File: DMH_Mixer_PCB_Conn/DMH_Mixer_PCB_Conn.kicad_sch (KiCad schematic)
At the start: 0 parts

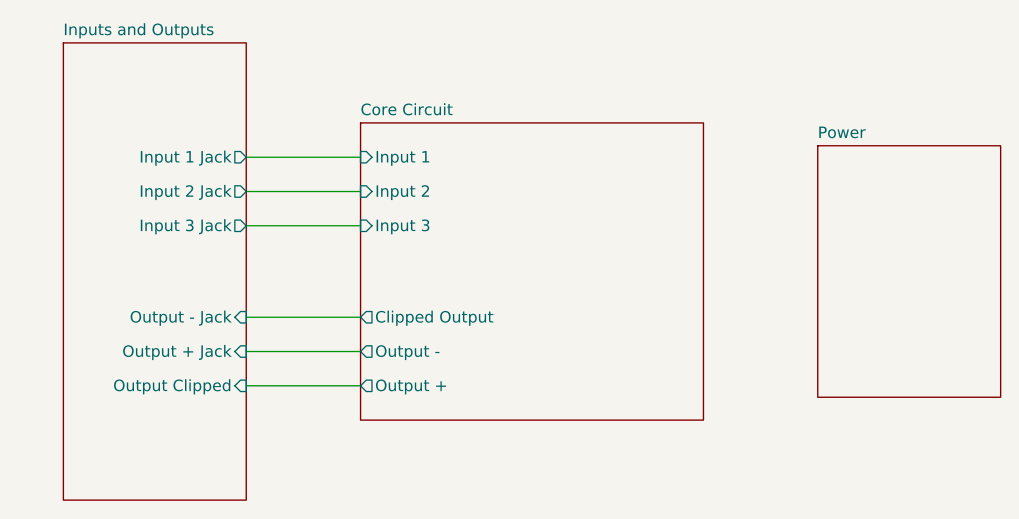
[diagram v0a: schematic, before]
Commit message: Adapted connectors PCB to 4 channel
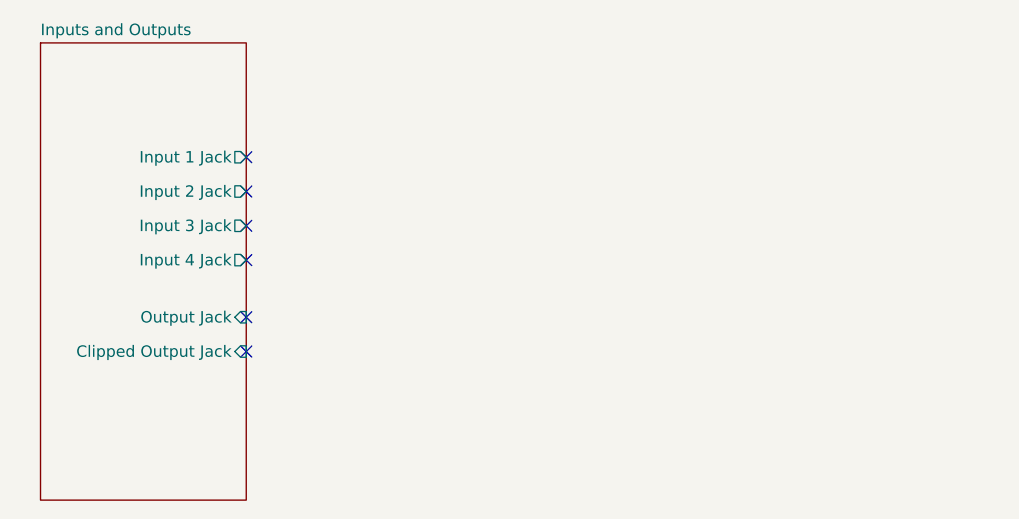
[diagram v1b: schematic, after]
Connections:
- no-connect marks 0 -> 6
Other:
- removed sheet Core Circuit
- removed sheet Power
- sheet Inputs and Outputs ports: added Clipped Output Jack, Input 4 Jack, Output Jack; removed Output + Jack, Output - Jack, Output Clipped
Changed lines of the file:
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@@
 		(comment 1 "PCB for 5 cm Kosmo format synthesizer module")
 	)
-	(wire
-		(pts
-			(xy 38.1 88.9) (xy 50.8 88.9)
-		)
-		(stroke
-			(width 0)
-			(type default)
-		)
+	(no_connect
+		(at 38.1 96.52)
 	)
-	(wire
-		(pts
-			(xy 38.1 114.3) (xy 50.8 114.3)
-		)
-		(stroke
-			(width 0)
-			(type default)
-		)
+	(no_connect
+		(at 38.1 100.33)
 	)
-	(wire
-		(pts
-			(xy 38.1 92.71) (xy 50.8 92.71)
-		)
-		(stroke
-			(width 0)
-			(type default)
-		)
+	(no_connect
+		(at 38.1 88.9)
 	)
-	(wire
-		(pts
-			(xy 38.1 96.52) (xy 50.8 96.52)
-		)
-		(stroke
-			(width 0)
-			(type default)
-		)
+	(no_connect
+		(at 38.1 106.68)
 	)
-	(wire
-		(pts
-			(xy 38.1 110.49) (xy 50.8 110.49)
-		)
-		(stroke
-			(width 0)
-			(type default)
-		)
+	(no_connect
+		(at 38.1 92.71)
 	)
-	(wire
-		(pts
-			(xy 38.1 106.68) (xy 50.8 106.68)
-		)
-		(stroke
-			(width 0)
-			(type default)
-		)
+	(no_connect
+		(at 38.1 110.49)
 	)
 	(sheet
-		(at 101.6 87.63)
-		(size 20.32 27.94)
-		(fields_autoplaced yes)
-		(stroke
-			(width 0.1524)
-			(type solid)
-		)
-		(fill
-			(color 0 0 0 0.0000)
-		)
-		(property "Sheetname" "Power"
-			(at 101.6 86.9184 0)
-			(effects
-				(font
-					(size 1.27 1.27)
-				)
-				(justify left bottom)
-			)
-		)
-		(property "Sheetfile" "Power.kicad_sch"
-			(at 101.6 116.1546 0)
-			(effects
-				(font
-					(size 1.27 1.27)
-				)
-				(justify left top)
-				(hide yes)
-			)
-		)
-		(instances
-			(project "DMH_Mixer_PCB_Conn"
-				(path "/58f4306d-5387-4983-bb08-41a2313fd315"
-					(page "4")
-				)
-			)
-		)
-	)
-	(sheet
-		(at 50.8 85.09)
-		(size 38.1 33.02)
-		(fields_autoplaced yes)
-		(stroke
-			(width 0.1524)
-			(type solid)
-		)
-		(fill
-			(color 0 0 0 0.0000)
-		)
-		(property "Sheetname" "Core Circuit"
-			(at 50.8 84.3784 0)
-			(effects
-				(font
-					(size 1.27 1.27)
-				)
-				(justify left bottom)
-			)
-		)
-		(property "Sheetfile" "Core_Circuit.kicad_sch"
-			(at 50.8 118.6946 0)
-			(effects
-				(font
-					(size 1.27 1.27)
-				)
-				(justify left top)
-				(hide yes)
-			)
-		)
-		(pin "Input 3" input
-			(at 50.8 96.52 180)
-			(effects
-				(font
-					(size 1.27 1.27)
-				)
-				(justify left)
-			)
-		)
-		(pin "Input 1" input
-			(at 50.8 88.9 180)
-			(effects
-				(font
-					(size 1.27 1.27)
-				)
-				(justify left)
-			)
-		)
-		(pin "Input 2" input
-			(at 50.8 92.71 180)
-			(effects
-				(font
-					(size 1.27 1.27)
-				)
-				(justify left)
-			)
-		)
-		(pin "Clipped Output" output
-			(at 50.8 106.68 180)
-			(effects
-				(font
-					(size 1.27 1.27)
-				)
-				(justify left)
-			)
-		)
-		(pin "Output -" output
-			(at 50.8 110.49 180)
-			(effects
-				(font
-					(size 1.27 1.27)
-				)
-				(justify left)
-			)
-		)
-		(pin "Output +" output
-			(at 50.8 114.3 180)
-			(effects
-				(font
-					(size 1.27 1.27)
-				)
-				(justify left)
-			)
-		)
-		(instances
-			(project "DMH_Mixer_PCB_Conn"
-				(path "/58f4306d-5387-4983-bb08-41a2313fd315"
-					(page "3")
-				)
-			)
-		)
-	)
-	(sheet
-		(at 17.78 76.2)
-		(size 20.32 50.8)
+		(at 15.24 76.2)
+		(size 22.86 50.8)
 		(fields_autoplaced yes)
 		(stroke
@@
 		)
 		(property "Sheetname" "Inputs and Outputs"
-			(at 17.78 75.4884 0)
+			(at 15.24 75.4884 0)
 			(effects
 				(font
@@
 		)
 		(property "Sheetfile" "Inputs_and_Outputs.kicad_sch"
-			(at 17.78 127.5846 0)
+			(at 15.24 127.5846 0)
 			(effects
 				(font
@@
 			)
 		)
-		(pin "Output - Jack" input
+		(pin "Output Jack" input
 			(at 38.1 106.68 0)
 			(effects
@@
 			)
 		)
-		(pin "Output + Jack" input
+		(pin "Clipped Output Jack" input
 			(at 38.1 110.49 0)
 			(effects
@@
 			)
 		)
-		(pin "Output Clipped" input
-			(at 38.1 114.3 0)
+		(pin "Input 4 Jack" output
+			(at 38.1 100.33 0)
 			(effects
 				(font

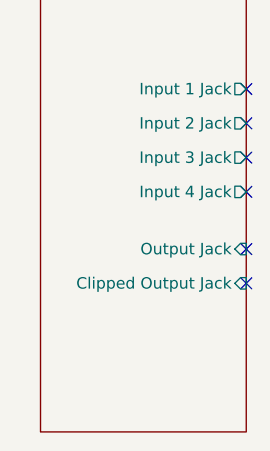
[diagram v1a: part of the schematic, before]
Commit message: Panel and Connectors PCB ready
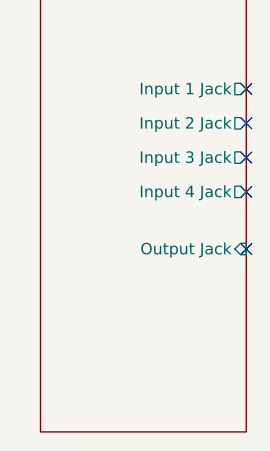
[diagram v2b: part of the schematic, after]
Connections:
- no-connect marks 6 -> 5
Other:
- sheet Inputs and Outputs ports: added none; removed Clipped Output Jack
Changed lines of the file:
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@@
 		(at 38.1 92.71)
-	)
-	(no_connect
-		(at 38.1 110.49)
 	)
 	(sheet
@@
 			(effects
 				(font
-					(size 1.27 1.27)
-				)
-				(justify right)
-			)
-		)
-		(pin "Clipped Output Jack" input
-			(at 38.1 110.49 0)
-			(effects
-				(font
